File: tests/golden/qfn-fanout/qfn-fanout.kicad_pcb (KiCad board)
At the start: 2 copper layers, 44 x 40 mm, 8 parts, among them J1 CONN_ISP_1X06, J2 CONN_BRK_1X04, U1 ATMEGA328P_QFN32

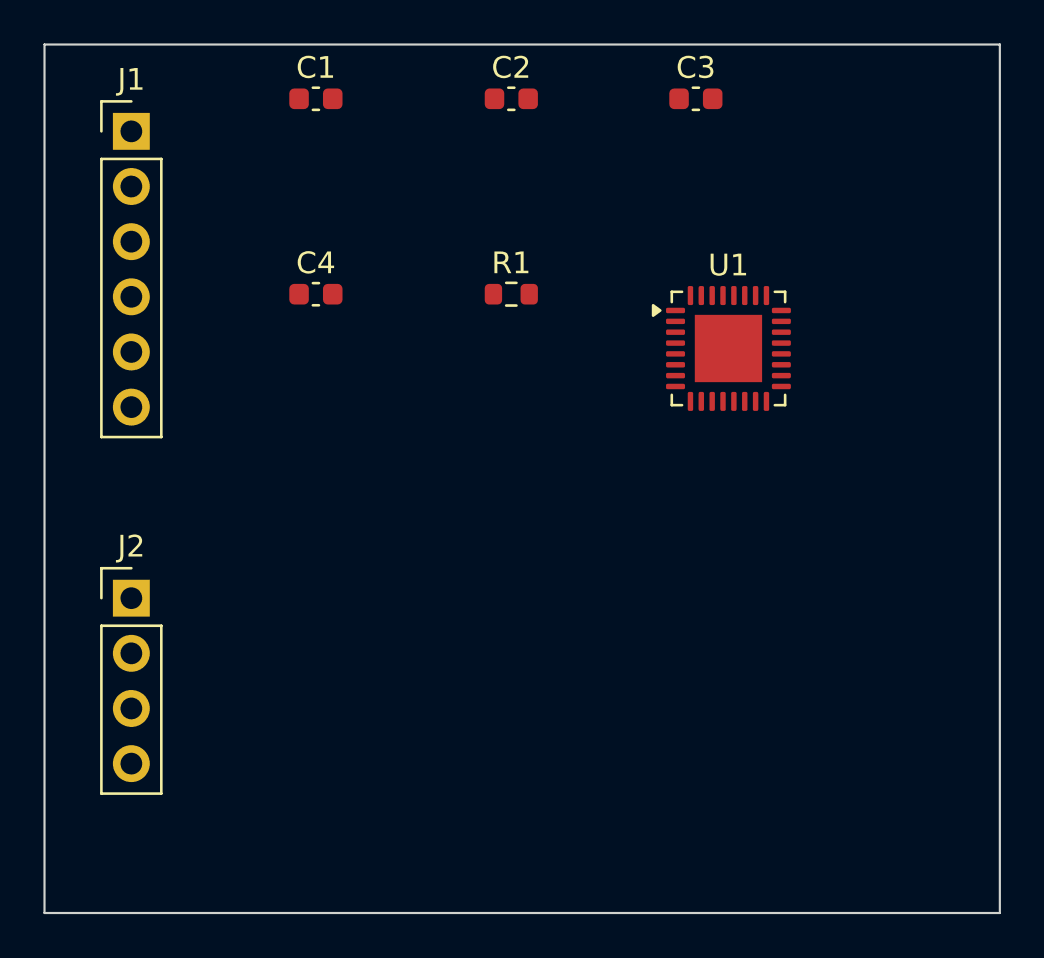
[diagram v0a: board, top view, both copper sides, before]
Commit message: M10: copper pours, stitching vias and plane integrity
Pours are source intent now: `pours:` says which net owns the free copper of
which layer, with priorities where two zones share one, thermal or solid pad
connection, per-pad-instance overrides, island-removal rules and a fragmentation
threshold. `stitching:` generates the vias that tie the pours together -- grid,
edge or ring -- as a deterministic pattern, in the architecture M9e established
for fanout escapes.

What aipcb emits is the zone and never the fill. KiCad's own engine produces the
copper, because KiCad's fill is what DRC checks against and a second
implementation would differ on every board (ADR 0009). `kicad-cli` 9.0.8 cannot
fill, so the engine is reached through a `pcbnew` subprocess with a version lock:
it refuses to fill unless pcbnew and kicad-cli report the same KiCad, and a fill
that fails is a check failure with pcbnew's stderr attached, never a quietly
unfilled board.

The split that makes this safe: `aipcb build` stays a byte-stable pure function
of the source with its zones unfilled, and `aipcb check` and `aipcb export` fill
a staged copy. An unfilled pour exports as no copper at all, silently, which is
why a failed fill stops the run instead of falling back.

After the fill, `aipcb check` reads the filled polygons back and reports what the
copper actually came out as -- islands, largest-island fraction, bounding boxes,
and what island removal deleted, measured by filling a second time with removal
off rather than inferred. `min_contiguous:` turns fragmentation into a warning
and never an error.

Eight of the ten examples gain a pour; `congestion` and `overconstrained` have no
ground net at all and keep none, which is also the live witness that a design
without `pours:` builds byte-identically. Four examples stitch. All ten pass
kicad-cli's DRC with zero violations on the board that was actually checked.

Three defects surfaced and are fixed: a stitching via drilled 0.21 mm from a
routed vi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
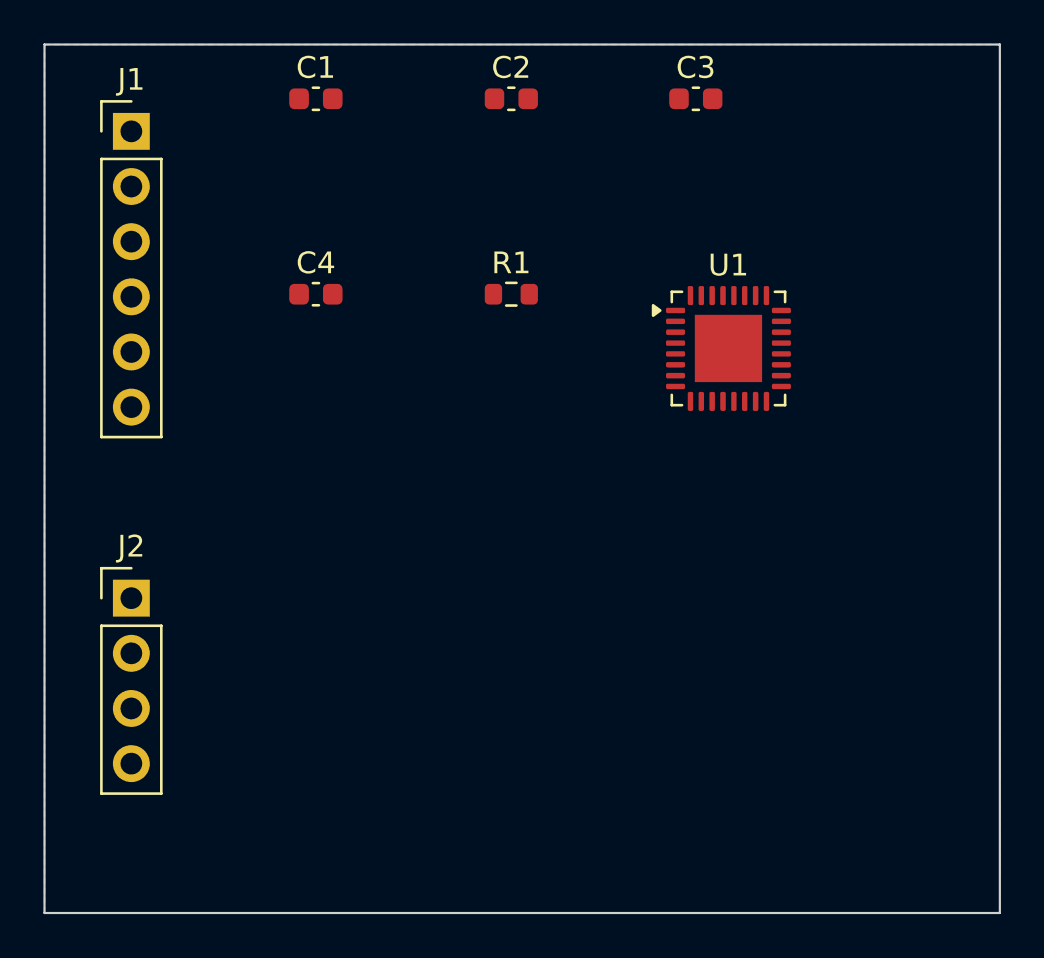
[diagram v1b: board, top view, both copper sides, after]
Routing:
- added copper zone on B.Cu, net GND
- added copper zone on F.Cu, net GND
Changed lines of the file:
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@@
 			(property pad_prop_heatsink)
 			(layers "F.Cu" "F.Mask")
+			(net 2 "GND")
 			(zone_connect 2)
-			(net 2 "GND")
 		)
 		(embedded_fonts no)
@@
 		(layer "Edge.Cuts")
 	)
+	(zone
+		(net 2)
+		(net_name "GND")
+		(layers "F.Cu" "B.Cu")
+		(hatch edge 0.5)
+		(connect_pads
+			(clearance 0.15)
+		)
+		(min_thickness 0.25)
+		(filled_areas_thickness no)
+		(fill yes
+			(thermal_gap 0.25)
+			(thermal_bridge_width 0.5)
+		)
+		(polygon
+			(pts
+				(xy 100 100)
+				(xy 144 100)
+				(xy 144 140)
+				(xy 100 140)
+			)
+		)
+	)
 	(embedded_fonts no)
